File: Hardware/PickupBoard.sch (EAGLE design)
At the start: 29 parts, among them T1 2N3904, U1 TL074_

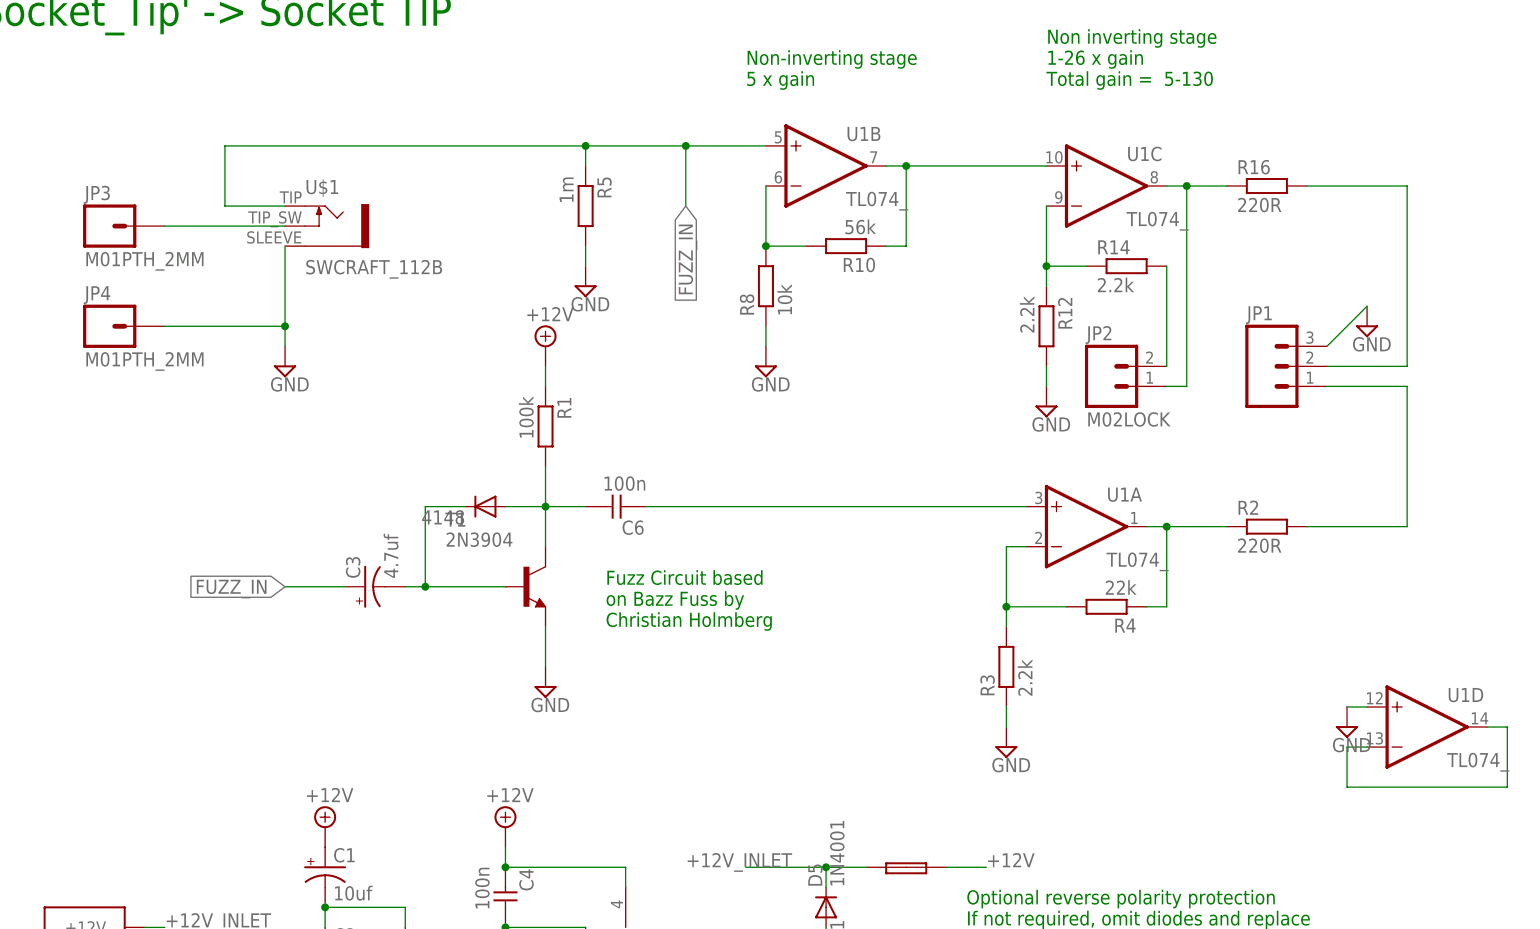
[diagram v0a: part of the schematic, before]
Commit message: Rev2 Pickup Board finished and routed
Panel and Daughterboard unchanged fixes #2, fixes #3, fixes #4
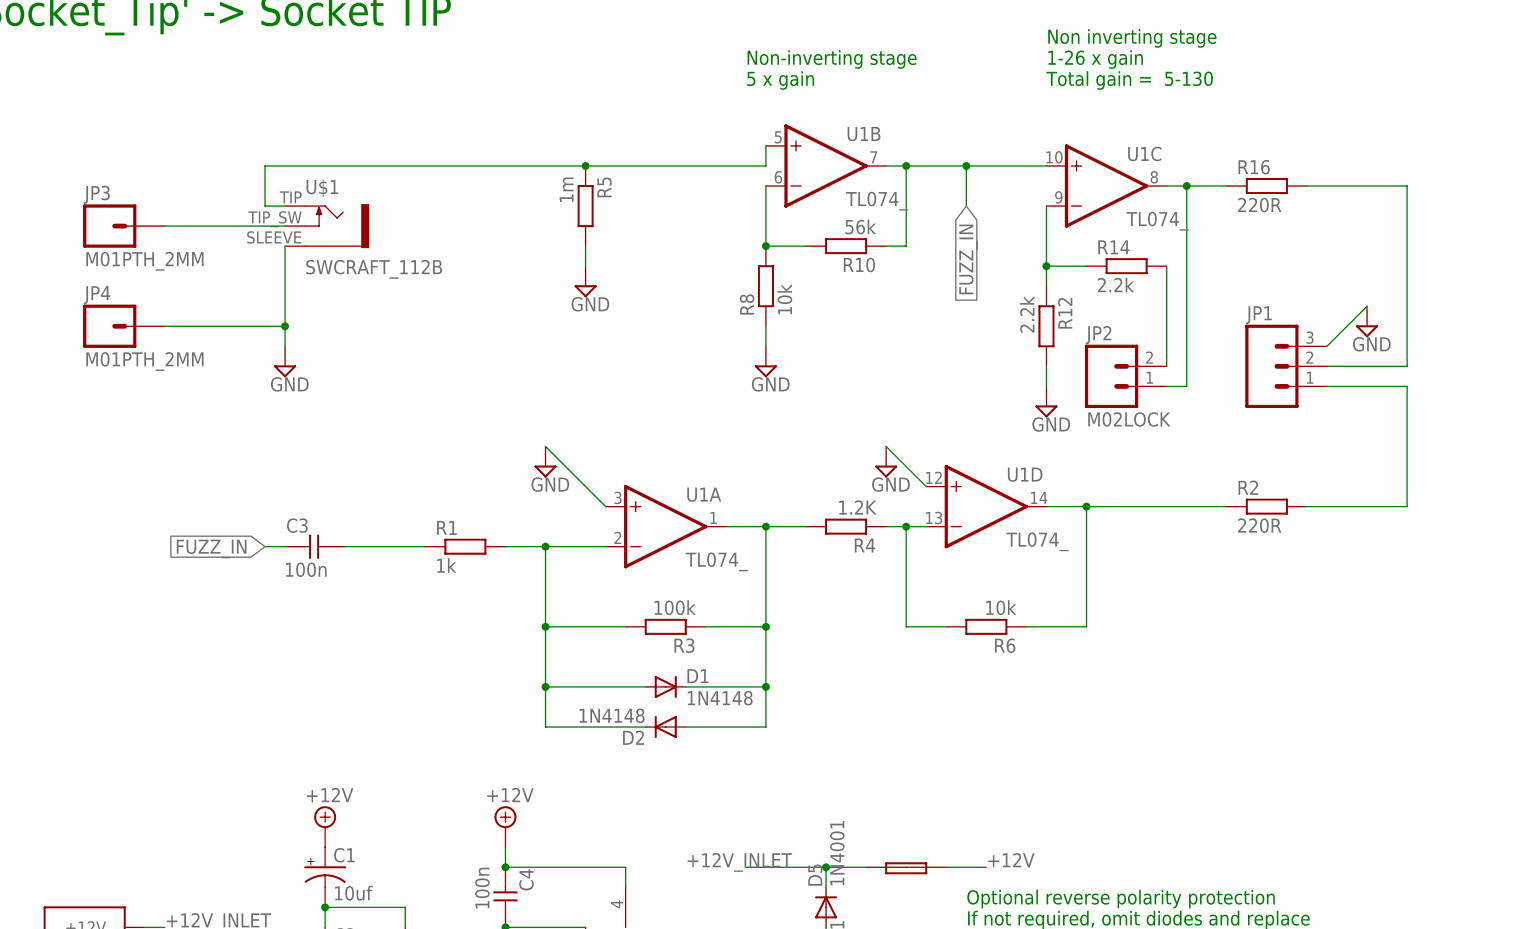
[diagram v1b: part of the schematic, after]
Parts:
- removed 4148: (no value), MusicThingModular:SMALL_DIODEDO35-7
- removed C6: 100n, TomW:C-EU050-024X044
- removed T1: 2N3904, transistor:2N3904
- added D1, D2: 1N4148, MusicThingModular:SMALL_DIODEDO35-7
- added R6: 10k, MusicThingModular:RESISTOR7MM
- C3: value 4.7uf -> 100n; device SparkFun-Passives:CAP_POLPTH2 -> TomW:C-EU050-024X044
- R1: value 100k -> 1k
- R3: value 2.2k -> 100k
- R4: value 22k -> 1.2K
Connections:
- removed net N$12: R2.1, R4.1, U1A.OUT
- net +12V: no longer R1.1
- net FUZZ_IN: now also C3.2, R10.1, U1B.OUT, U1C.+IN; no longer C3.+, R5.1, U$1.3, U1B.+IN
- net GND: now also U1A.+IN; no longer R3.1, T1.E
- net N$1: now also R5.1, U$1.3, U1B.+IN; no longer C6.2, U1A.+IN
- net N$11: now also R2.1, R6.1, U1D.OUT; no longer R3.2, R4.2, U1A.-IN
- net N$2: now also D1.C, D2.A, R3.1, R4.2, U1A.OUT; no longer U1D.-IN, U1D.OUT
- net N$4: now also D1.A, D2.C, R1.2, R3.2, U1A.-IN; no longer R10.1, U1B.OUT, U1C.+IN
- net N$7: now also C3.1, R1.1; no longer 4148.C, C3.-, T1.B
- net N$9: now also R4.1, R6.2, U1D.-IN; no longer 4148.A, C6.1, R1.2, T1.C
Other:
- note removed: "Fuzz Circuit based on Bazz Fuss by Christian Holmberg"
- moved on the sheet: R1, R2, R3, R4, U1A, U1D

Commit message: notes for changes to fix high frequency oscillation
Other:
- note added: "Try 10k here"
- note added: "replace 100k with 470pf cap R4 = 10k R6 = 100k"
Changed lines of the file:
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@@
 PCB 'Socket_Slv' -&gt; Socket SLEEVE
 PCB 'Socket_Tip' -&gt; Socket TIP </text>
+<text x="73.66" y="71.12" size="1.778" layer="91">Try 10k here </text>
+<text x="127" y="55.88" size="1.778" layer="91">replace 100k with 470pf cap
+R4 = 10k
+R6 = 100k </text>
 </plain>
 <instances>

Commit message: Value changes + new cap
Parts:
- removed R3: 100k, MusicThingModular:RESISTOR7MM
- added C6: 470pf, TomW:C-EU050-024X044
- C3: value 100n -> 470n
- R1: value 1k -> 10k
- R4: value 1.2K -> 10k
- R6: value 10k -> 100k
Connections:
- net N$2: now also C6.1; no longer R3.1
- net N$4: now also C6.2; no longer R3.2
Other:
- note removed: "Try 10k here"
- note removed: "replace 100k with 470pf cap R4 = 10k R6 = 100k"
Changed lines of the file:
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@@
 <?xml version="1.0" encoding="utf-8"?>
 <!DOCTYPE eagle SYSTEM "eagle.dtd">
-<eagle version="7.4.0">
+<eagle version="7.2.0">
 <drawing>
 <settings>
@@
 <part name="SUPPLY20" library="supply2" deviceset="GND" device=""/>
 <part name="FRAME1" library="frames" deviceset="A4L-LOC" device=""/>
-<part name="C3" library="TomW" deviceset="C-EU" device="050-024X044" value="100n"/>
+<part name="C3" library="TomW" deviceset="C-EU" device="050-024X044" value="470n"/>
 <part name="U1" library="MusicThingModular" deviceset="TL074" device="_"/>
 <part name="R2" library="MusicThingModular" deviceset="RESISTOR" device="7MM" value="220R"/>
@@
 <part name="JP3" library="SparkFun-Connectors" deviceset="M01" device="PTH_2MM"/>
 <part name="JP4" library="SparkFun-Connectors" deviceset="M01" device="PTH_2MM"/>
-<part name="R1" library="MusicThingModular" deviceset="RESISTOR" device="7MM" value="1k"/>
+<part name="R1" library="MusicThingModular" deviceset="RESISTOR" device="7MM" value="10k"/>
 <part name="SUPPLY1" library="supply2" deviceset="GND" device=""/>
 <part name="D1" library="MusicThingModular" deviceset="SMALL_DIODE" device="DO35-7" value="1N4148"/>
 <part name="D2" library="MusicThingModular" deviceset="SMALL_DIODE" device="DO35-7" value="1N4148"/>
-<part name="R3" library="MusicThingModular" deviceset="RESISTOR" device="7MM" value="100k"/>
-<part name="R4" library="MusicThingModular" deviceset="RESISTOR" device="7MM" value="1.2K"/>
+<part name="C6" library="TomW" deviceset="C-EU" device="050-024X044" value="470pf"/>
+<part name="R4" library="MusicThingModular" deviceset="RESISTOR" device="7MM" value="10k"/>
 <part name="SUPPLY2" library="supply2" deviceset="GND" device=""/>
-<part name="R6" library="MusicThingModular" deviceset="RESISTOR" device="7MM" value="10k"/>
+<part name="R6" library="MusicThingModular" deviceset="RESISTOR" device="7MM" value="100k"/>
 </parts>
 <sheets>
@@
 PCB 'Socket_Slv' -&gt; Socket SLEEVE
 PCB 'Socket_Tip' -&gt; Socket TIP </text>
-<text x="73.66" y="71.12" size="1.778" layer="91">Try 10k here </text>
-<text x="127" y="55.88" size="1.778" layer="91">replace 100k with 470pf cap
-R4 = 10k
-R6 = 100k </text>
 </plain>
 <instances>
@@
 <instance part="D1" gate="G$1" x="109.22" y="60.96"/>
 <instance part="D2" gate="G$1" x="109.22" y="55.88" rot="R180"/>
-<instance part="R3" gate="G$1" x="109.22" y="68.58" rot="R180"/>
+<instance part="C6" gate="G$1" x="109.22" y="68.58" rot="R270"/>
 <instance part="R4" gate="G$1" x="132.08" y="81.28" rot="R180"/>
 <instance part="SUPPLY2" gate="GND" x="137.16" y="88.9"/>
@@
 <wire x1="93.98" y1="55.88" x2="93.98" y2="60.96" width="0.1524" layer="91"/>
 <junction x="93.98" y="60.96"/>
-<pinref part="R3" gate="G$1" pin="2"/>
+<pinref part="C6" gate="G$1" pin="2"/>
 <wire x1="104.14" y1="68.58" x2="93.98" y2="68.58" width="0.1524" layer="91"/>
 <junction x="93.98" y="68.58"/>
@@
 <wire x1="121.92" y1="55.88" x2="121.92" y2="60.96" width="0.1524" layer="91"/>
 <junction x="121.92" y="60.96"/>
-<pinref part="R3" gate="G$1" pin="1"/>
-<wire x1="114.3" y1="68.58" x2="121.92" y2="68.58" width="0.1524" layer="91"/>
+<pinref part="C6" gate="G$1" pin="1"/>
+<wire x1="111.76" y1="68.58" x2="121.92" y2="68.58" width="0.1524" layer="91"/>
 <junction x="121.92" y="68.58"/>
 <pinref part="R4" gate="G$1" pin="2"/>
